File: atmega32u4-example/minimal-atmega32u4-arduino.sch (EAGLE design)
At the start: 32 parts, among them U1 MCP73831, U2 MIC5219, U3 32U4, X1 USB-MICROB, Y1 8MHz

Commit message: Finished layout and BOM of ATMEGA32u4 board. Uses mostly the same parts as the 328 board now.
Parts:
- removed JP1: JST-2, SparkFun-Connectors:M02-JST-2MM-SMT
- removed JP2, JP3: FIDUCIALUFIDUCIAL, SparkFun:FIDUCIALUFIDUCIAL
- removed LED1, LED2, LED3, LED4: RED, SparkFun-LED:LED0603
- removed R7: 330, SparkFun-Passives:RESISTOR0603-RES
- removed S1: SWITCH-DPDTSMD, SparkFun-Electromechanical:SWITCH-DPDTSMD
- removed S2: !RESET, SparkFun-Electromechanical:SWITCH-MOMENTARY-2SMD
- removed X1: USB-MICROB, SparkFun-Connectors:USB-MICROB
- removed Y1: 8MHz, SparkFun-FreqCtrl:RESONATORSMD
- added C10, C11, C18: 100n, rcl:C-EUC0805K
- added C16, C17: 18p, rcl:C-EUC0805K
- added C19: 4.7u, rcl:C-EUC0805K
- added D2, D3, D5, D6, D7: GREEN, led:LEDCHIP-LED0805
- added D4: B340A, SparkFun-DiscreteSemi:DIODE-SCHOTTKY_
- added H1, H2, H3, H4: STAND-OFF, SparkFun-Hardware:STAND-OFF
- added J1: 3x2 M, SmartPrj:PINHD-2X3
- added J2: S2B-PH-SM4-TB(LF)(SN), SparkFun-Connectors:M02-JST-2MM-SMT
- added J3: 629105136821, Wurth_Elektronik_Electromechanic_Input-Output_Connectors_rev19b:629105136821
- added R10, R11, R12: 1K, rcl:R-US_R0805
- added SW1: AYZ0202AGRLC, SparkFun-Electromechanical:SWITCH-DPDTSMD
- added SW2: !RESET, SparkFun-Electromechanical:SWITCH-MOMENTARY-2SMD
- added TP3: TPPAD1-13, testpad:TPPAD1-13
- added X2: 16 MHz, SparkFun-Clocks:CRYSTALSMD-HC49UP
- C1: value 470pF -> 470p; device SparkFun-Passives:CAP0603-CAP -> rcl:C-EUC0805K; DESC (none) -> CAP CER 470PF 50V X7R 0805; MFR (none) -> Samsung; MPN (none) -> CL21B471KBANNNC; PROD_ID CAP-07884 -> (none)
- C2, C3, C4: value .1uF -> 100n; device SparkFun-Passives:CAP0603-CAP -> rcl:C-EUC0805K; DESC (none) -> CAP CER 0.1UF 50V X7R 0805; MFR (none) -> Samsung; MPN (none) -> CL21B104KBCNNNC; PROD_ID CAP-00810 -> (none)
- C5: value 1uF -> 1u; device SparkFun-Passives:CAP0603-CAP -> rcl:C-EUC0805K; DESC (none) -> CAP CER 1UF 16V X7R 0805; MFR (none) -> Samsung; MPN (none) -> CL21B105KOFNNNG; PROD_ID CAP-00868 -> (none)
- C6: value 4.7uF -> 4.7u; device SparkFun-Passives:CAP0603-CAP -> rcl:C-EUC0805K; DESC (none) -> CAP CER 4.7UF 16V X5R 0805; MFR (none) -> Samsung; MPN (none) -> CL21A475KOFNNNE; PROD_ID CAP-08280 -> (none)
- C7, C8: value 4.7uF -> 4.7u; device SparkFun-Passives:CAP1206 -> rcl:C-EUC0805K; DESC (none) -> CAP CER 4.7UF 16V X5R 0805; MFR (none) -> Samsung; MPN (none) -> CL21A475KOFNNNE; PROD_ID CAP-10300 -> (none)
- C9: value 4.7uF -> 100n; device SparkFun-Passives:CAP1206 -> rcl:C-EUC0805K; DESC (none) -> CAP CER 0.1UF 50V X7R 0805; MFR (none) -> Samsung; MPN (none) -> CL21B104KBCNNNC; PROD_ID CAP-10300 -> (none)
- D1: DESC (none) -> DIODE SCHOTTKY 40V 2A SMA; MFR (none) -> Diodes Inc; MPN (none) -> B340AE-13; PROD_ID DIO-09886 -> (none)
- R1, R8: value 330 -> 1K; device SparkFun-Passives:RESISTOR0603-RES -> rcl:R-US_R0805; DESC (none) -> RES SMD 1K OHM 1% 1/8W 0805; MFR (none) -> Yageo; MPN (none) -> RC0805FR-071KL; PROD_ID RES-00818 -> (none)
- R2, R3: value 10k -> 10K; device SparkFun-Passives:RESISTOR0603-RES -> rcl:R-US_R0805; DESC (none) -> RES SMD 10K OHM 1% 1/8W 0805; MFR (none) -> Yageo; MPN (none) -> RC0805FR-0710KL; PROD_ID RES-00824 -> (none)
- R4, R5: device SparkFun-Passives:RESISTOR0603-RES -> rcl:R-US_R0805; DESC (none) -> RES SMD 22 OHM 1% 1/8W 0805; MFR (none) -> Yageo; MPN (none) -> RC0805FR-0722RL; PROD_ID RES-08698 -> (none)
- R6: value 330 -> 10K; device SparkFun-Passives:RESISTOR0603-RES -> rcl:R-US_R0805; DESC (none) -> RES SMD 10K OHM 1% 1/8W 0805; MFR (none) -> Yageo; MPN (none) -> RC0805FR-0710KL; PROD_ID RES-00818 -> (none)
- U1: DESC (none) -> IC CONTROLLR LI-ION 4.2V SOT23-5; MFR (none) -> Microchip; MPN (none) -> MCP73831T-2ACI/OT
- U2: DESC (none) -> IC REG LINEAR 3.3V 500MA SOT23-5; MFR (none) -> Microchip; MPN (none) -> MIC5219-3.3YM5-TR; PROD_ID VREG-09872 -> (none)
- U3: value 32U4 -> ATMEGA32U4-AUR; DESC (none) -> IC MCU 8BIT 32KB FLASH 44TQFP; MFR (none) -> Microchip; MPN (none) -> ATMEGA32U4-AUR
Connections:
- net N$6 renamed MCPPROG
- net N$8 renamed MIC-BP
- removed net 5V: C7.2, C9.2, D1.C, R1.2, S1.1, U1.VIN, U2.IN, U3.VBUS, X1.VBUS
- removed net MISO: U3.PB3(MISO)
- removed net MOSI: U3.PB2(MOSI)
- removed net N$1: LED2.C, R6.1
- removed net N$18: LED4.A, R8.1
- removed net N$2: S1.2, U2.EN
- removed net N$21: LED3.C, R7.1
- removed net N$5: U3.XTAL1, Y1.1
- removed net RESET: R3.2, S2.2, U3.!RESET
- removed net RX_LED: R6.2, U3.PB0(SS)
- removed net SCK: U3.PB1(SCK)
- removed net USER_LED: R8.2, U3.PC7
- new net !RESET: J1.5, R3.1, SW2.2, TP3.TP, U3.!RESET
- new net AREF: C4.1, U3.AREF
- new net D13#/USER_LED: R11.2, U3.PC7
- new net D14/MISO: J1.1, U3.PB3(MISO)
- new net D15/SCK: J1.3, U3.PB1(SCK)
- new net D16/MOSI: J1.4, U3.PB2(MOSI)
- new net D17/RX-LED: D6.C, U3.PB0(SS)
- new net MIC-EN: SW1.2, U2.EN
- new net N$13: D3.A, R11.1
- new net N$14: C18.1, J3.SHIELD
- new net N$15: D6.A, R8.1
- new net N$16: D7.A, R12.1
- new net PE2/!HWB: R6.2, U3.PE2/!HWB
- new net PWRIN: C7.1, D1.C, D4.C, SW1.1, U2.IN
- new net UCAP: C5.1, U3.UCAP
- new net VBUS: C19.1, D4.A, J3.VBUS, R1.2, U1.VIN, U3.UVCC, U3.VBUS
- new net XTAL1: C17.1, U3.XTAL1, X2.2
- new net XTAL2: C16.1, U3.XTAL2, X2.1
- net 3.3V: now also C10.1, C11.1, C2.1, C3.1, C8.1, C9.1, J1.2, R10.2, R12.2, R3.2, R8.2; no longer C2.2, C3.2, C4.2, C5.2, C6.2, LED2.A, LED3.A, R3.1, U3.AREF, U3.UCAP
- net D+: now also R5.2; no longer R4.1
- net D-: now also R4.2; no longer R5.1
- net GND: now also C10.2, C11.2, C16.2, C17.2, C18.2, C19.2, C2.2, C3.2, C4.2, C5.2, C6.2, C7.2, C8.2, C9.2, D2.C, D3.C, J1.6, J2.2, J3.GND, R6.1, SW1.3, SW2.1; no longer C2.1, C3.1, C4.1, C5.1, C6.1, C7.1, C8.1, C9.1, JP1.2, LED4.C, S1.3, S2.1, U3.PE2/!HWB, X1.GND, Y1.2
- net N$19: now also J3.D-, R4.1; no longer R5.2, X1.D-
- net N$20: now also J3.D+, R5.1; no longer R4.2, X1.D+
- net N$3: now also D5.A; no longer LED1.A
- net N$4: now also D5.C; no longer LED1.C
- net N$7: now also D2.A, R10.1; no longer U3.XTAL2, Y1.3
- net TX_LED: now also D7.C; no longer R7.2
- net V_BATT: now also C6.1, J2.1; no longer C8.2, JP1.1
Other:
- note added: "1"
- note added: "A0"
- note added: "A1"
- note added: "A2"
- note added: "A3"
- note added: "A4"
- note added: "A5"
- note added: "D0"
- note added: "D1"
- note added: "D10#"
- note added: "D11#"
- note added: "D12/A10"
- note added: "D2"
- note added: "D3#"
- note added: "D4/A6"
- note added: "D5#"
- note added: "D6#/A7"
- note added: "D7"
- note added: "D8"
- note added: "D9#/A8"
- note added: "ICSP"
- note added: "M3 / #4-40 mounting holes"
- note added: "Originally taken from Arduino Lilypad Rev 10 Licensed under Creative Commons Attribution ShareAlike (CC BY-SA)"
- note added: "POWER"
- note added: "REQUIRED to program ATMEGA328P"
- note added: "USB RX"
- note added: "USB TX"
- note added: "USER"
- note removed: "10"
- note removed: "32u4 BYPASS"
- note removed: "L. Buechly and N. Seidle"
- note removed: "Mike Hord"
- note removed: "Original Lilypad Design by:"
- note removed: "Reduced by Andrew G."

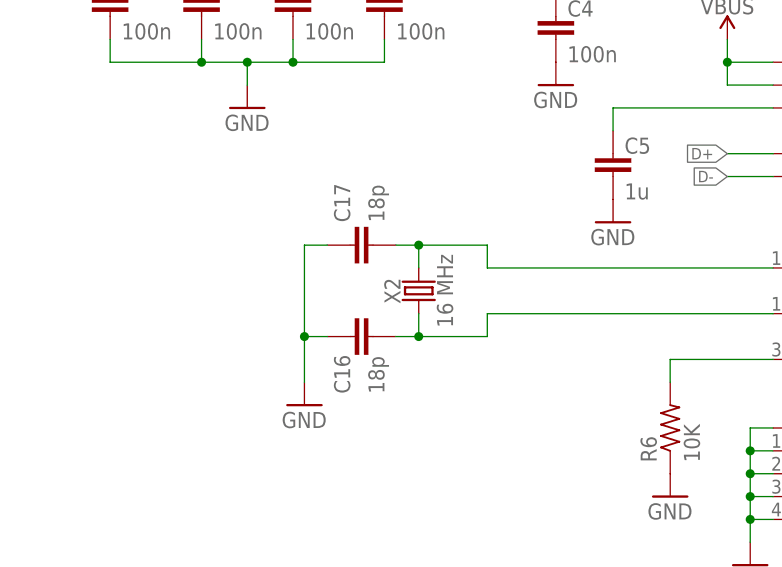
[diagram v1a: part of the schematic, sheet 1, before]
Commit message: Eeek! Bad cap values for the crystal oscillator. Changed from 18pF to 30 pF based on 18 pF load cap and 0805 capacitors.
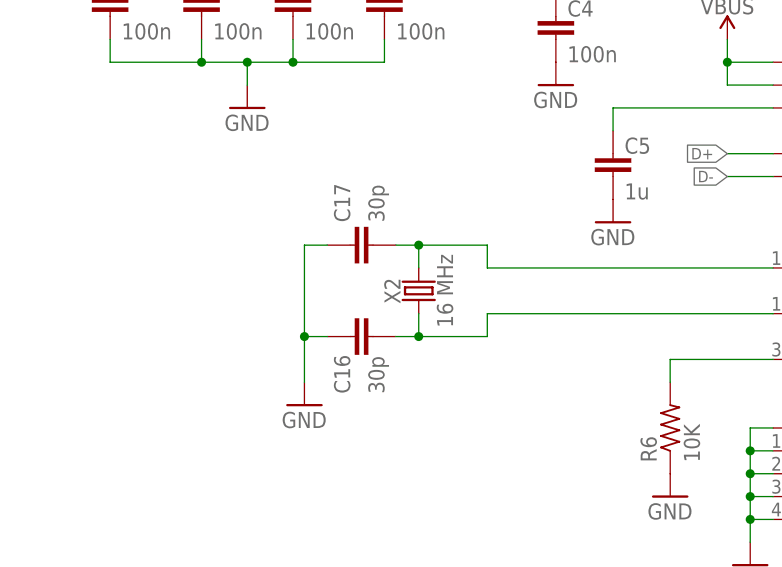
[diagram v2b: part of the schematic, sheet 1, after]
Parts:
- C16: value 18p -> 30p; DESC CAP CER 18PF 50V C0G/NP0 0805 -> CAP CER 30PF 50V C0G/NP0 0805; MPN CL21C180JBANNNC -> CL21C300JBANNNC
- C17: value 18p -> 30p; DESC CAP CER 18PF 50V C0G/NP0 0805 -> CAP CER 30PF 50V C0G/NP0 0805
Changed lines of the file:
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@@
 <attribute name="MPN" value="ECS-160-18-5PX-TR"/>
 </part>
-<part name="C16" library="rcl" library_urn="urn:adsk.eagle:library:334" deviceset="C-EU" device="C0805K" package3d_urn="urn:adsk.eagle:package:23681/2" value="18p">
-<attribute name="DESC" value="CAP CER 18PF 50V C0G/NP0 0805"/>
+<part name="C16" library="rcl" library_urn="urn:adsk.eagle:library:334" deviceset="C-EU" device="C0805K" package3d_urn="urn:adsk.eagle:package:23681/2" value="30p">
+<attribute name="DESC" value="CAP CER 30PF 50V C0G/NP0 0805"/>
+<attribute name="MFR" value="Samsung"/>
+<attribute name="MPN" value="CL21C300JBANNNC"/>
+</part>
+<part name="C17" library="rcl" library_urn="urn:adsk.eagle:library:334" deviceset="C-EU" device="C0805K" package3d_urn="urn:adsk.eagle:package:23681/2" value="30p">
+<attribute name="DESC" value="CAP CER 30PF 50V C0G/NP0 0805"/>
 <attribute name="MFR" value="Samsung"/>
 <attribute name="MPN" value="CL21C180JBANNNC"/>
-</part>
-<part name="C17" library="rcl" library_urn="urn:adsk.eagle:library:334" deviceset="C-EU" device="C0805K" package3d_urn="urn:adsk.eagle:package:23681/2" value="18p">
-<attribute name="DESC" value="CAP CER 18PF 50V C0G/NP0 0805"/>
-<attribute name="MFR" value="Samsung"/>
-<attribute name="MPN" value="CL21C180JBANNNC"/>

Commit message: Better setup instructions.
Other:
- note added: "REQUIRED to program ATMEGA32U4"
- note removed: "REQUIRED to program ATMEGA328P"
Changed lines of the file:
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@@
 <setting verticaltext="up"/>
 </settings>
-<grid distance="0.1" unitdist="inch" unit="inch" style="lines" multiple="1" display="no" altdistance="0.01" altunitdist="inch" altunit="inch"/>
+<grid distance="0.05" unitdist="inch" unit="inch" style="lines" multiple="2" display="no" altdistance="0.01" altunitdist="inch" altunit="inch"/>
 <layers>
 <layer number="1" name="Top" color="4" fill="1" visible="no" active="no"/>
@@
 <wire x1="365.76" y1="90.17" x2="320.04" y2="90.17" width="0.1524" layer="97"/>
 <text x="339.09" y="63.5" size="2.54" layer="97">ICSP</text>
-<text x="322.58" y="60.96" size="1.778" layer="97">REQUIRED to program ATMEGA328P</text>
+<text x="321.31" y="60.96" size="1.778" layer="97">REQUIRED to program ATMEGA32U4</text>
 <text x="269.24" y="77.47" size="1.778" layer="97" rot="R90">USB RX</text>
 <text x="293.37" y="77.47" size="1.778" layer="97" rot="R90">USB TX</text>
